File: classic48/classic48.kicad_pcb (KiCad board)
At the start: 2 copper layers, 144.6 x 71 mm, 75 parts, among them SW1 Switch, SW10 Switch, SW11 Switch, SW12 Switch, SW13 Switch, SW14 Switch, SW15 Switch, SW16 Switch, SW17 Switch, SW18 Switch, SW19 Switch, SW2 Switch, SW20 Switch, SW21 Switch, SW22 Switch, SW23 Switch, SW24 Switch, SW3 Switch, SW4 Switch, SW5 Switch, SW6 Switch, SW7 Switch, SW8 Switch, SW9 Switch, U1 RP2040_Pro_Micro, U2 TRRS

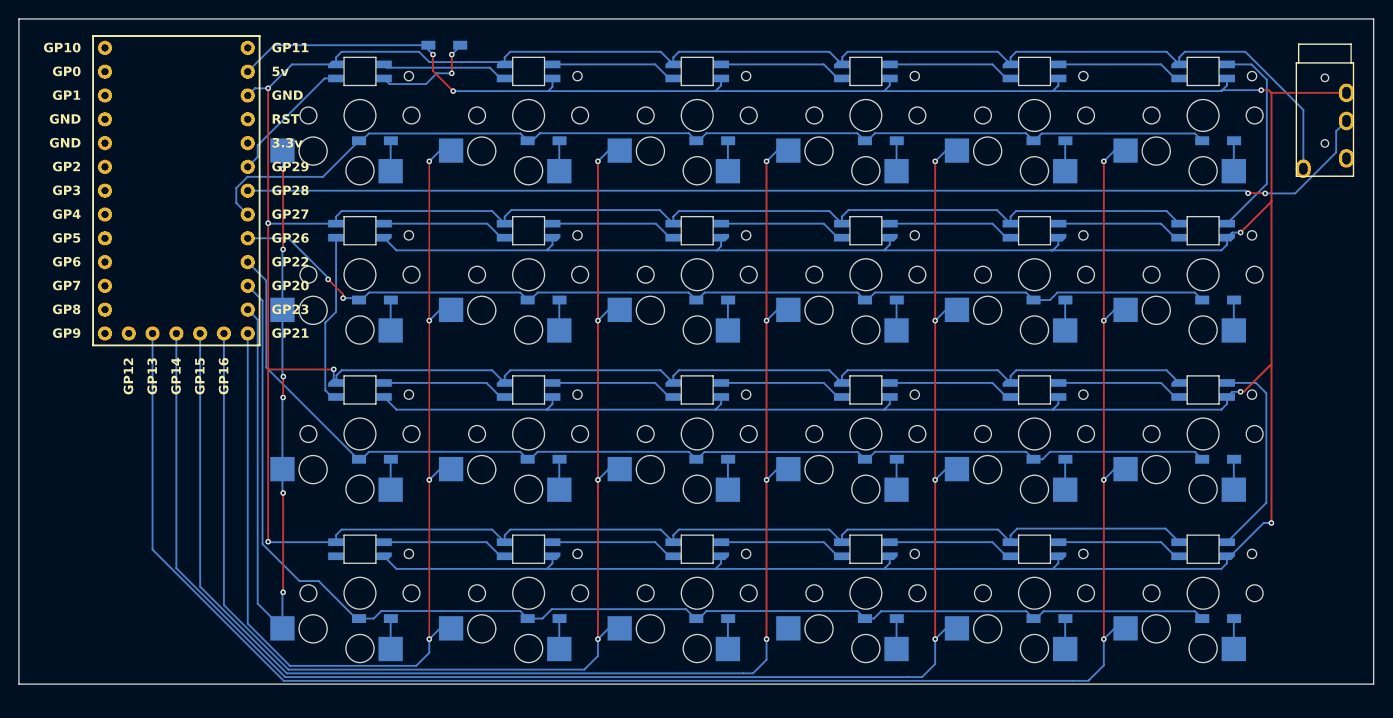
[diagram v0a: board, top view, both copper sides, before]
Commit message: fix: DRC errors except LEDS
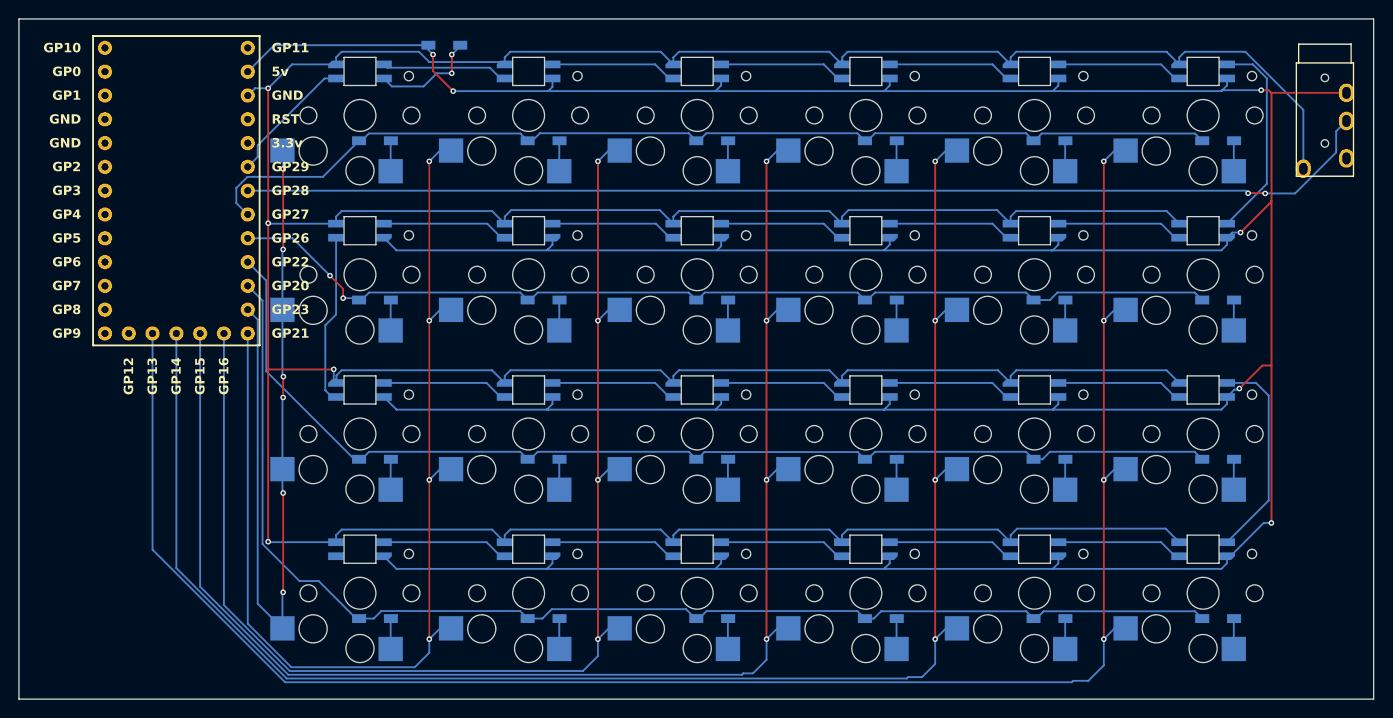
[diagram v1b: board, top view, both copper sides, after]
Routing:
- net Col 3 Left: track 153.5 -> 156.4 mm
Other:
- board size 144.6 x 71 mm -> 144.6 x 72.6 mm

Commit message: feat: improve silk screen pin placement for 2040
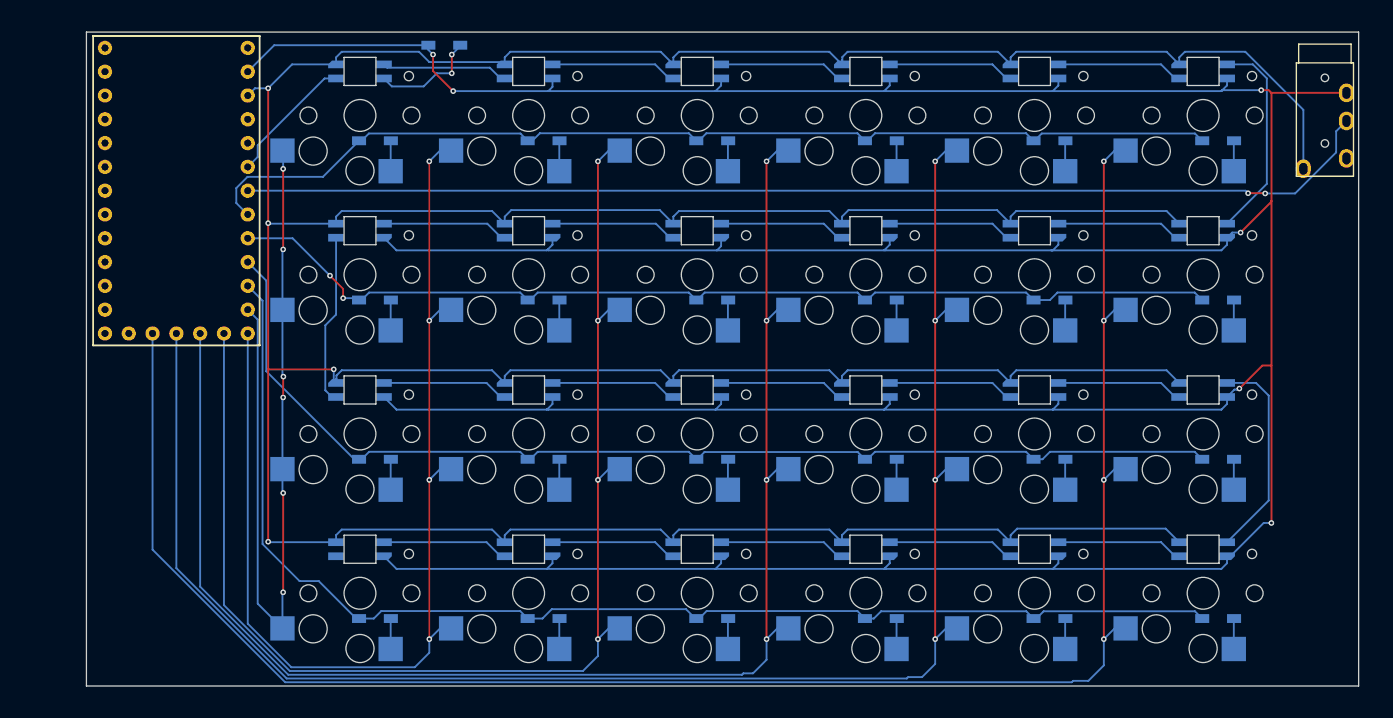
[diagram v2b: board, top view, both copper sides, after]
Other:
- board size 144.6 x 72.6 mm -> 135.8 x 69.8 mm

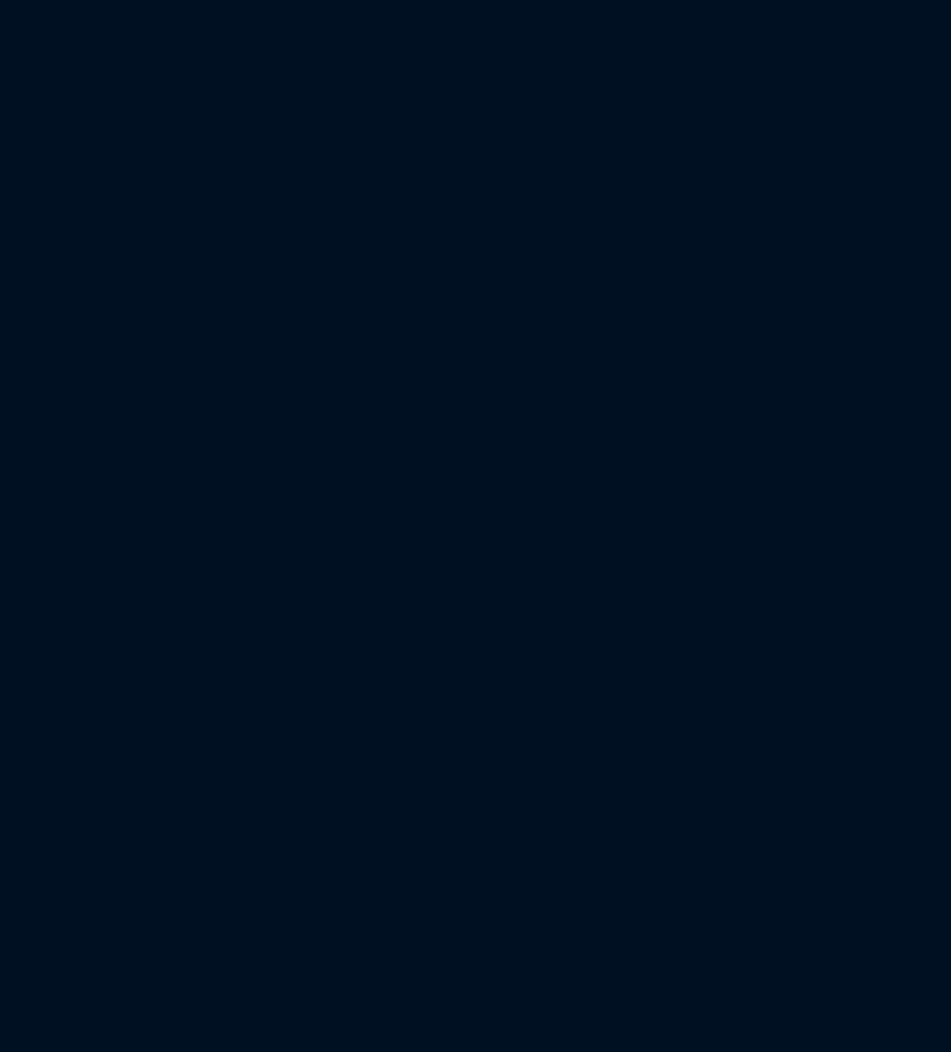
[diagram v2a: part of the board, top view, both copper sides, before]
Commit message: fix: left side LEDs were connected incorrectly feat: right side schema
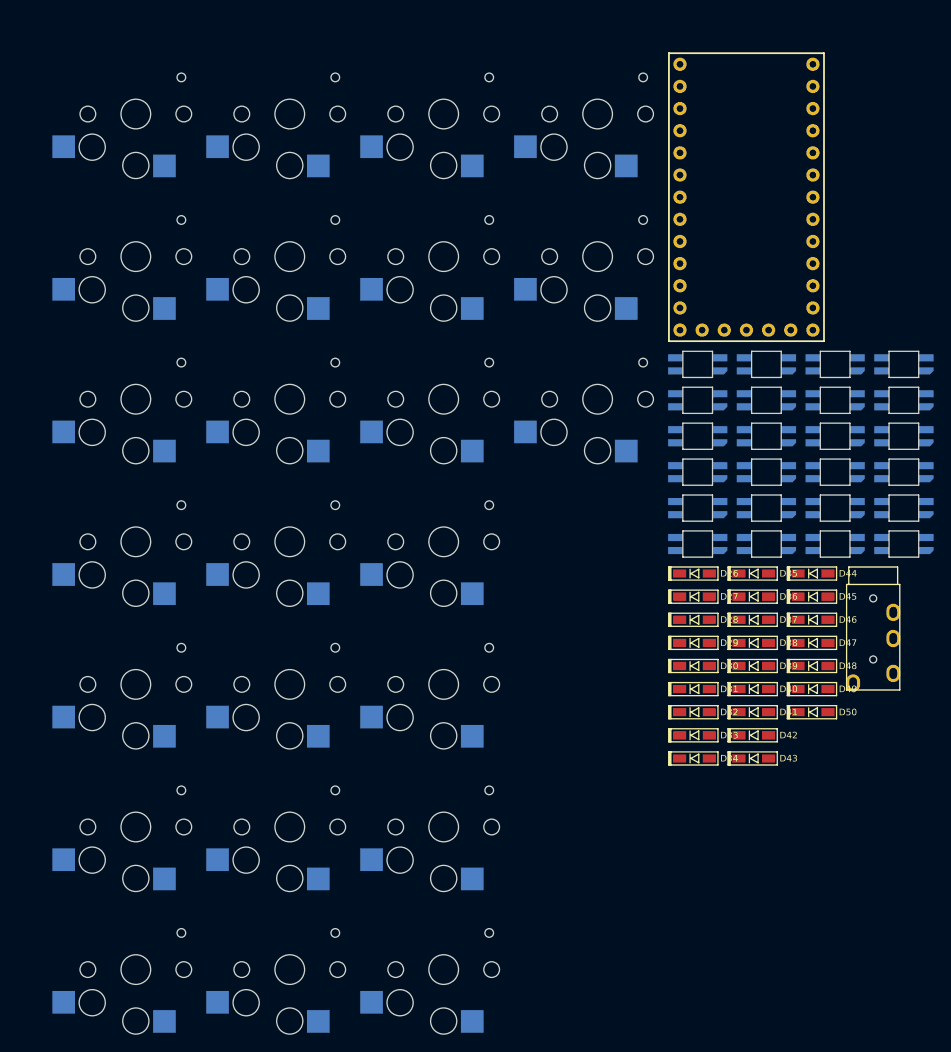
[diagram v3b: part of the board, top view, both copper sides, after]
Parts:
- added D26: Diode_1N4148-SOD123, pjimenez:Diode_1N4148-SOD123, F.Cu at (296.4, 90.2)
- added D27: Diode_1N4148-SOD123, pjimenez:Diode_1N4148-SOD123, F.Cu at (296.4, 92.9)
- added D28: Diode_1N4148-SOD123, pjimenez:Diode_1N4148-SOD123, F.Cu at (296.4, 95.5)
- added D29: Diode_1N4148-SOD123, pjimenez:Diode_1N4148-SOD123, F.Cu at (296.4, 98.2)
- added D30: Diode_1N4148-SOD123, pjimenez:Diode_1N4148-SOD123, F.Cu at (296.4, 100.8)
- added D31: Diode_1N4148-SOD123, pjimenez:Diode_1N4148-SOD123, F.Cu at (296.4, 103.5)
- added D32: Diode_1N4148-SOD123, pjimenez:Diode_1N4148-SOD123, F.Cu at (296.4, 106.1)
- added D33: Diode_1N4148-SOD123, pjimenez:Diode_1N4148-SOD123, F.Cu at (296.4, 108.8)
- added D34: Diode_1N4148-SOD123, pjimenez:Diode_1N4148-SOD123, F.Cu at (296.4, 111.4)
- added D35: Diode_1N4148-SOD123, pjimenez:Diode_1N4148-SOD123, F.Cu at (303.2, 90.2)
- added D36: Diode_1N4148-SOD123, pjimenez:Diode_1N4148-SOD123, F.Cu at (303.2, 92.9)
- added D37: Diode_1N4148-SOD123, pjimenez:Diode_1N4148-SOD123, F.Cu at (303.2, 95.5)
- added D38: Diode_1N4148-SOD123, pjimenez:Diode_1N4148-SOD123, F.Cu at (303.2, 98.2)
- added D39: Diode_1N4148-SOD123, pjimenez:Diode_1N4148-SOD123, F.Cu at (303.2, 100.8)
- added D40: Diode_1N4148-SOD123, pjimenez:Diode_1N4148-SOD123, F.Cu at (303.2, 103.5)
- added D41: Diode_1N4148-SOD123, pjimenez:Diode_1N4148-SOD123, F.Cu at (303.2, 106.1)
- added D42: Diode_1N4148-SOD123, pjimenez:Diode_1N4148-SOD123, F.Cu at (303.2, 108.8)
- added D43: Diode_1N4148-SOD123, pjimenez:Diode_1N4148-SOD123, F.Cu at (303.2, 111.4)
- added D44: Diode_1N4148-SOD123, pjimenez:Diode_1N4148-SOD123, F.Cu at (310.0, 90.2)
- added D45: Diode_1N4148-SOD123, pjimenez:Diode_1N4148-SOD123, F.Cu at (310.0, 92.9)
- added D46: Diode_1N4148-SOD123, pjimenez:Diode_1N4148-SOD123, F.Cu at (310.0, 95.5)
- added D47: Diode_1N4148-SOD123, pjimenez:Diode_1N4148-SOD123, F.Cu at (310.0, 98.2)
- added D48: Diode_1N4148-SOD123, pjimenez:Diode_1N4148-SOD123, F.Cu at (310.0, 100.8)
- added D49: Diode_1N4148-SOD123, pjimenez:Diode_1N4148-SOD123, F.Cu at (310.0, 103.5)
- added D50: Diode_1N4148-SOD123, pjimenez:Diode_1N4148-SOD123, F.Cu at (310.0, 106.1)
- added LED25: LED_SK6812MINI-E, pjimenez:LED_SK6812-MINI-E, F.Cu at (296.8, 66.2)
- added LED26: LED_SK6812MINI-E, pjimenez:LED_SK6812-MINI-E, F.Cu at (296.8, 70.4)
- added LED27: LED_SK6812MINI-E, pjimenez:LED_SK6812-MINI-E, F.Cu at (296.8, 74.5)
- added LED28: LED_SK6812MINI-E, pjimenez:LED_SK6812-MINI-E, F.Cu at (296.8, 78.6)
- added LED29: LED_SK6812MINI-E, pjimenez:LED_SK6812-MINI-E, F.Cu at (296.8, 82.7)
- added LED30: LED_SK6812MINI-E, pjimenez:LED_SK6812-MINI-E, F.Cu at (296.8, 86.8)
- added LED31: LED_SK6812MINI-E, pjimenez:LED_SK6812-MINI-E, F.Cu at (304.7, 66.2)
- added LED32: LED_SK6812MINI-E, pjimenez:LED_SK6812-MINI-E, F.Cu at (304.7, 70.4)
- added LED33: LED_SK6812MINI-E, pjimenez:LED_SK6812-MINI-E, F.Cu at (304.7, 74.5)
- added LED34: LED_SK6812MINI-E, pjimenez:LED_SK6812-MINI-E, F.Cu at (304.7, 78.6)
- added LED35: LED_SK6812MINI-E, pjimenez:LED_SK6812-MINI-E, F.Cu at (304.7, 82.7)
- added LED36: LED_SK6812MINI-E, pjimenez:LED_SK6812-MINI-E, F.Cu at (304.7, 86.8)
- added LED37: LED_SK6812MINI-E, pjimenez:LED_SK6812-MINI-E, F.Cu at (312.6, 66.2)
- added LED38: LED_SK6812MINI-E, pjimenez:LED_SK6812-MINI-E, F.Cu at (312.6, 70.4)
- added LED39: LED_SK6812MINI-E, pjimenez:LED_SK6812-MINI-E, F.Cu at (312.6, 74.5)
- added LED40: LED_SK6812MINI-E, pjimenez:LED_SK6812-MINI-E, F.Cu at (312.6, 78.6)
- added LED41: LED_SK6812MINI-E, pjimenez:LED_SK6812-MINI-E, F.Cu at (312.6, 82.7)
- added LED42: LED_SK6812MINI-E, pjimenez:LED_SK6812-MINI-E, F.Cu at (312.6, 86.8)
- added LED43: LED_SK6812MINI-E, pjimenez:LED_SK6812-MINI-E, F.Cu at (320.4, 66.2)
- added LED44: LED_SK6812MINI-E, pjimenez:LED_SK6812-MINI-E, F.Cu at (320.4, 70.4)
- added LED45: LED_SK6812MINI-E, pjimenez:LED_SK6812-MINI-E, F.Cu at (320.4, 74.5)
- added LED46: LED_SK6812MINI-E, pjimenez:LED_SK6812-MINI-E, F.Cu at (320.4, 78.6)
- added LED47: LED_SK6812MINI-E, pjimenez:LED_SK6812-MINI-E, F.Cu at (320.4, 82.7)
- added LED48: LED_SK6812MINI-E, pjimenez:LED_SK6812-MINI-E, F.Cu at (320.4, 86.8)
- added SW25: Switch, pjimenez:Switch_ChocV1-hotswap, F.Cu at (232.4, 37.5)
- added SW26: Switch, pjimenez:Switch_ChocV1-hotswap, F.Cu at (232.4, 53.9)
- added SW27: Switch, pjimenez:Switch_ChocV1-hotswap, F.Cu at (232.4, 70.2)
- added SW28: Switch, pjimenez:Switch_ChocV1-hotswap, F.Cu at (232.4, 86.6)
- added SW29: Switch, pjimenez:Switch_ChocV1-hotswap, F.Cu at (232.4, 102.9)
- added SW30: Switch, pjimenez:Switch_ChocV1-hotswap, F.Cu at (232.4, 119.3)
- added SW31: Switch, pjimenez:Switch_ChocV1-hotswap, F.Cu at (232.4, 135.6)
- added SW32: Switch, pjimenez:Switch_ChocV1-hotswap, F.Cu at (250.0, 37.5)
- added SW33: Switch, pjimenez:Switch_ChocV1-hotswap, F.Cu at (250.0, 53.9)
- added SW34: Switch, pjimenez:Switch_ChocV1-hotswap, F.Cu at (250.0, 70.2)
- added SW35: Switch, pjimenez:Switch_ChocV1-hotswap, F.Cu at (250.0, 86.6)
- added SW36: Switch, pjimenez:Switch_ChocV1-hotswap, F.Cu at (250.0, 102.9)
- added SW37: Switch, pjimenez:Switch_ChocV1-hotswap, F.Cu at (250.0, 119.3)
- added SW38: Switch, pjimenez:Switch_ChocV1-hotswap, F.Cu at (250.0, 135.6)
- added SW39: Switch, pjimenez:Switch_ChocV1-hotswap, F.Cu at (267.7, 37.5)
- added SW40: Switch, pjimenez:Switch_ChocV1-hotswap, F.Cu at (267.7, 53.9)
- added SW41: Switch, pjimenez:Switch_ChocV1-hotswap, F.Cu at (267.7, 70.2)
- added SW42: Switch, pjimenez:Switch_ChocV1-hotswap, F.Cu at (267.7, 86.6)
- added SW43: Switch, pjimenez:Switch_ChocV1-hotswap, F.Cu at (267.7, 102.9)
- added SW44: Switch, pjimenez:Switch_ChocV1-hotswap, F.Cu at (267.7, 119.3)
- added SW45: Switch, pjimenez:Switch_ChocV1-hotswap, F.Cu at (267.7, 135.6)
- added SW46: Switch, pjimenez:Switch_ChocV1-hotswap, F.Cu at (285.3, 37.5)
- added SW47: Switch, pjimenez:Switch_ChocV1-hotswap, F.Cu at (285.3, 53.9)
- added SW48: Switch, pjimenez:Switch_ChocV1-hotswap, F.Cu at (285.3, 70.2)
- added U3: RP2040_Pro_Micro, pjimenez:RP2040_Pro_Micro, F.Cu at (302.4, 48.4)
- added U4: TRRS, pjimenez:TRRS_PJ-320A, F.Cu at (316.9, 91.5)
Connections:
- net Serial data left renamed Serial data Left
- LED10 pad 1: GND Left -> 5V Left
- LED10 pad 3: 5V Left -> GND Left
- LED11 pad 1: GND Left -> 5V Left
- LED11 pad 3: 5V Left -> GND Left
- LED12 pad 1: GND Left -> 5V Left
- LED12 pad 3: 5V Left -> GND Left
- LED19 pad 1: GND Left -> 5V Left
- LED19 pad 3: 5V Left -> GND Left
- LED20 pad 1: GND Left -> 5V Left
- LED20 pad 3: 5V Left -> GND Left
- LED21 pad 1: GND Left -> 5V Left
- LED21 pad 3: 5V Left -> GND Left
- LED22 pad 1: GND Left -> 5V Left
- LED22 pad 3: 5V Left -> GND Left
- LED23 pad 1: GND Left -> 5V Left
- LED23 pad 3: 5V Left -> GND Left
- LED24 pad 1: GND Left -> 5V Left
- LED24 pad 3: 5V Left -> GND Left
- LED7 pad 1: GND Left -> 5V Left
- LED7 pad 3: 5V Left -> GND Left
- LED8 pad 1: GND Left -> 5V Left
- LED8 pad 3: 5V Left -> GND Left
- LED9 pad 1: GND Left -> 5V Left
- LED9 pad 3: 5V Left -> GND Left

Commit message: fix: LED connections
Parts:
- removed D26, D27, D28, D29, D30, D31, D32, D33, D34, D35, D36, D37, D38, D39, D40, D41, D42, D43, D44, D45, D46, D47, D48, D49, D50: Diode_1N4148-SOD123, pjimenez:Diode_1N4148-SOD123
- removed LED25, LED26, LED27, LED28, LED29, LED30, LED31, LED32, LED33, LED34, LED35, LED36, LED37, LED38, LED39, LED40, LED41, LED42, LED43, LED44, LED45, LED46, LED47, LED48: LED_SK6812MINI-E, pjimenez:LED_SK6812-MINI-E
- removed SW25, SW26, SW27, SW28, SW29, SW30, SW31, SW32, SW33, SW34, SW35, SW36, SW37, SW38, SW39, SW40, SW41, SW42, SW43, SW44, SW45, SW46, SW47, SW48: Switch, pjimenez:Switch_ChocV1-hotswap
- removed U3: RP2040_Pro_Micro, pjimenez:RP2040_Pro_Micro
- removed U4: TRRS, pjimenez:TRRS_PJ-320A
- moved D25 6.30 mm to (66.0, 29.3), turned to 90 degrees
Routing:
- net Col 0 Left: track 86.8 -> 65.6 mm, vias 6 -> 4
- net Col 1 Left: track 116.6 -> 99.0 mm, vias 4 -> 5
- net Col 3 Left: track 156.4 -> 138.9 mm, vias 4 -> 5
- net Col 5 Left: track 196.2 -> 178.7 mm, vias 4 -> 5
- net Col 4 Left: track 176.4 -> 159.0 mm, vias 4 -> 5
- net Col 2 Left: track 136.5 -> 119.1 mm, vias 4 -> 5
- net Serial data Left: track 122.0 -> 139.0 mm, vias 2 -> 1
- net GND Left: track 496.8 -> 489.6 mm, vias 4 -> 0
- net 5V Left: track 488.3 -> 493.6 mm, vias 6 -> 3
- net Row 0 Left: track 111.8 -> 108.4 mm
- net Net-(D25-K): track 11.6 -> 8.29 mm, vias 2 -> 0
- net Net-(LED12-DOUT): track 18.2 -> 21.2 mm
- net Net-(LED6-DOUT): track 22.1 -> 23.1 mm
- net Net-(LED18-DOUT): track 22.5 -> 23.2 mm
- net Row 1 Left: track 108.5 -> 109.0 mm
